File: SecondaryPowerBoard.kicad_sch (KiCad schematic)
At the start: 0 parts

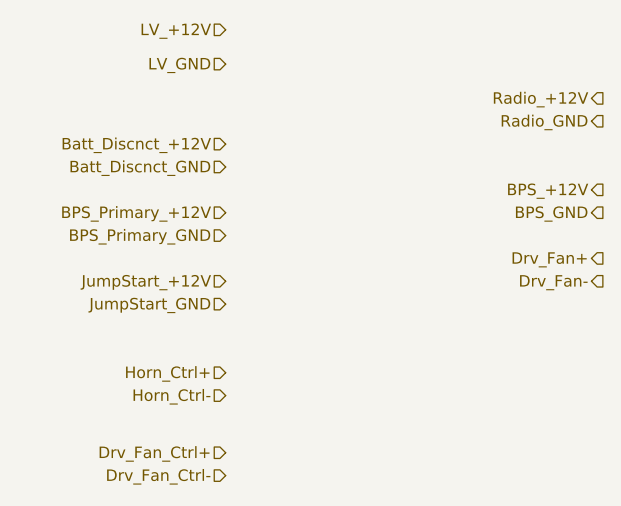
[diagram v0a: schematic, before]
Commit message: Updated Power Board wiring
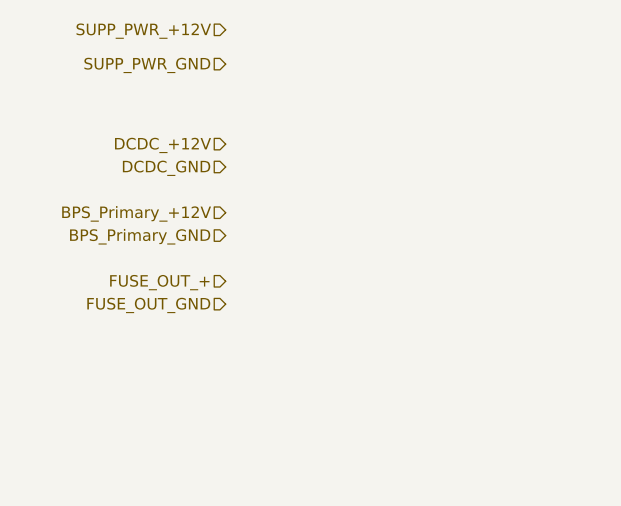
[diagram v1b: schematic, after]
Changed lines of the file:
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@@
 (kicad_sch (version 20230121) (generator eeschema)
   (paper "A4")
-  (hierarchical_label "LV_GND" (shape input) (at 88.9 67.31 180) (fields_autoplaced)
+  (hierarchical_label "SUPP_PWR_GND" (shape input) (at 88.9 67.31 180) (fields_autoplaced)
     (effects (font (size 1.27 1.27)) (justify right))
   )
-  (hierarchical_label "Batt_Discnct_GND" (shape input) (at 88.9 78.74 180) (fields_autoplaced)
+  (hierarchical_label "DCDC_GND" (shape input) (at 88.9 78.74 180) (fields_autoplaced)
     (effects (font (size 1.27 1.27)) (justify right))
   )
-  (hierarchical_label "Radio_GND" (shape output) (at 130.81 73.66 180) (fields_autoplaced)
-    (effects (font (size 1.27 1.27)) (justify right))
-  )
-  (hierarchical_label "BPS_+12V" (shape output) (at 130.81 81.28 180) (fields_autoplaced)
-    (effects (font (size 1.27 1.27)) (justify right))
-  )
-  (hierarchical_label "JumpStart_GND" (shape input) (at 88.9 93.98 180) (fields_autoplaced)
+  (hierarchical_label "FUSE_OUT_GND" (shape input) (at 88.9 93.98 180) (fields_autoplaced)
     (effects (font (size 1.27 1.27)) (justify right))
   )
@@
     (effects (font (size 1.27 1.27)) (justify right))
   )
-  (hierarchical_label "Drv_Fan-" (shape output) (at 130.81 91.44 180) (fields_autoplaced)
-    (effects (font (size 1.27 1.27)) (justify right))
-  )
   (hierarchical_label "BPS_Primary_+12V" (shape input) (at 88.9 83.82 180) (fields_autoplaced)
     (effects (font (size 1.27 1.27)) (justify right))
   )
-  (hierarchical_label "Radio_+12V" (shape output) (at 130.81 71.12 180) (fields_autoplaced)
+  (hierarchical_label "SUPP_PWR_+12V" (shape input) (at 88.9 63.5 180) (fields_autoplaced)
     (effects (font (size 1.27 1.27)) (justify right))
   )
-  (hierarchical_label "LV_+12V" (shape input) (at 88.9 63.5 180) (fields_autoplaced)
+  (hierarchical_label "FUSE_OUT_+" (shape input) (at 88.9 91.44 180) (fields_autoplaced)
     (effects (font (size 1.27 1.27)) (justify right))
   )
-  (hierarchical_label "Drv_Fan_Ctrl+" (shape input) (at 88.9 110.49 180) (fields_autoplaced)
+  (hierarchical_label "DCDC_+12V" (shape input) (at 88.9 76.2 180) (fields_autoplaced)
     (effects (font (size 1.27 1.27)) (justify right))
   )
-  (hierarchical_label "Drv_Fan_Ctrl-" (shape input) (at 88.9 113.03 180) (fields_autoplaced)
-    (effects (font (size 1.27 1.27)) (justify right))
-  )
-  (hierarchical_label "Horn_Ctrl+" (shape input) (at 88.9 101.6 180) (fields_autoplaced)
-    (effects (font (size 1.27 1.27)) (justify right))
-  )
-  (hierarchical_label "JumpStart_+12V" (shape input) (at 88.9 91.44 180) (fields_autoplaced)
-    (effects (font (size 1.27 1.27)) (justify right))
-  )
-  (hierarchical_label "Batt_Discnct_+12V" (shape input) (at 88.9 76.2 180) (fields_autoplaced)
-    (effects (font (size 1.27 1.27)) (justify right))
-  )
-  (hierarchical_label "BPS_GND" (shape output) (at 130.81 83.82 180) (fields_autoplaced)
-    (effects (font (size 1.27 1.27)) (justify right))
-  )
-  (hierarchical_label "Horn_Ctrl-" (shape input) (at 88.9 104.14 180) (fields_autoplaced)
-    (effects (font (size 1.27 1.27)) (justify right))
-  )
-  (hierarchical_label "Drv_Fan+" (shape output) (at 130.81 88.9 180) (fields_autoplaced)
-    (effects (font (size 1.27 1.27)) (justify right))
-  )
